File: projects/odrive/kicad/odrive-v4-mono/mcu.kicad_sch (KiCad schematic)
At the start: 20 parts, among them J4 FTSH-105-01-L-DV-K, U16 TPD4E05U06, U2 STM32F405RGT6, Y1 8MHz

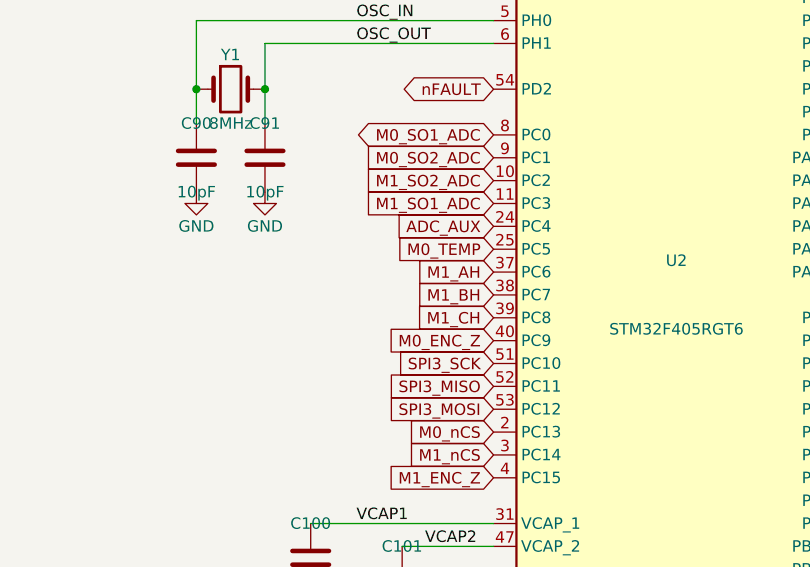
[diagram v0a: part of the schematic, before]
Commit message: Checkpoint ODrive 56 V recovery and modular handoff
Preserve corrected schematics, local libraries, partial PCB routing, firmware diagnostics, analysis tools and the independent modular-study handoff. The board remains incomplete with 381 unconnected items and 415 DRC warnings.

Validation: 52 host tests, ARM component compilation, schematic/PCB parity, native copper preservation, DRC, STEP export, Python lint, shellcheck and nix fmt. Known Konnect-generated schematic whitespace is retained. No fabrication or hardware validation is claimed.
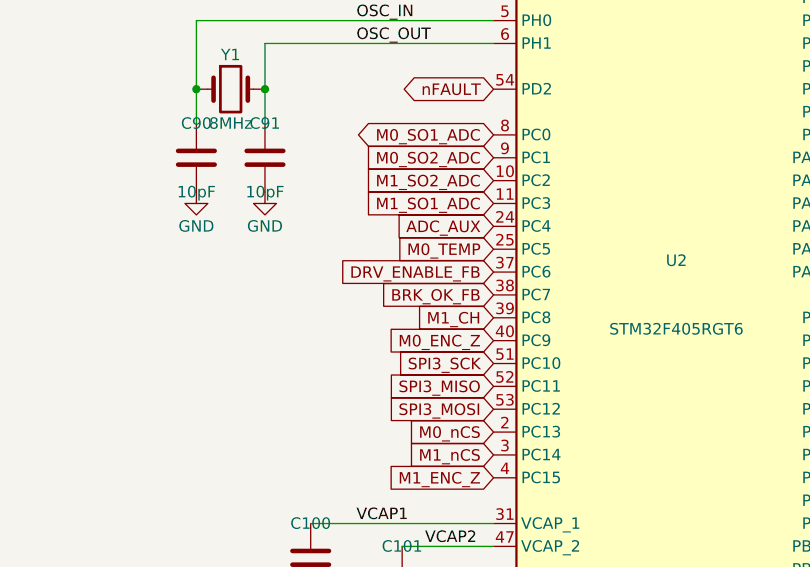
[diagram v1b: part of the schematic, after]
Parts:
- U2: Design_note (none) -> Mono firmware: PC6 is DRV_ENABLE_FB input with no pulls, no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
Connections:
- net M1_AH renamed DRV_ENABLE_FB
- net M1_BH renamed BRK_OK_FB
